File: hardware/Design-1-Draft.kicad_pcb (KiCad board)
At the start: 2 copper layers, 165 x 135 mm, 54 parts, among them J1 Barrel_Jack_Switch, M1 WP-1, M2 WP-2, Q1 IRLZ44N, Q2 IRLZ44N, Q3 PN2222A, SW1 Button, U3 ADS1115, U5 Tang_Nano_9K, U7 BOB-12009

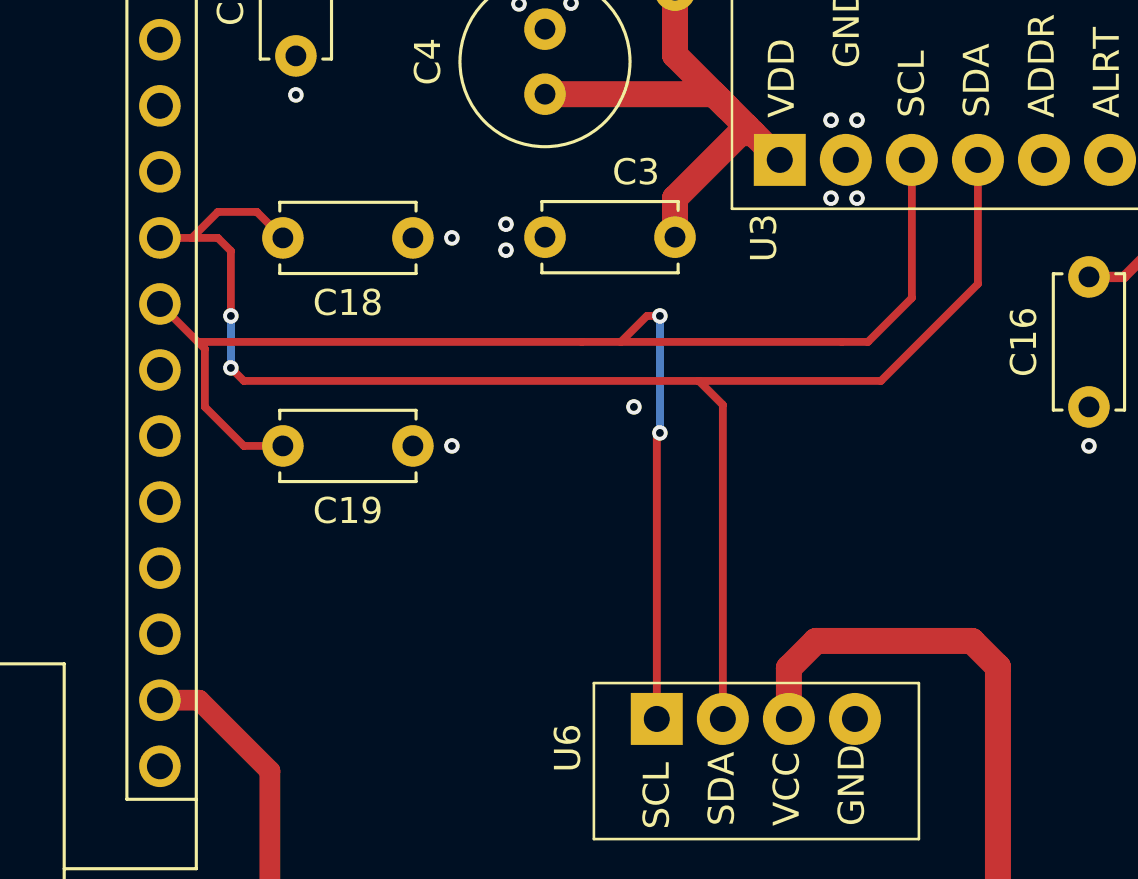
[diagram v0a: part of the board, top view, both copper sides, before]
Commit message: Updated schem & PCB, caps not removed
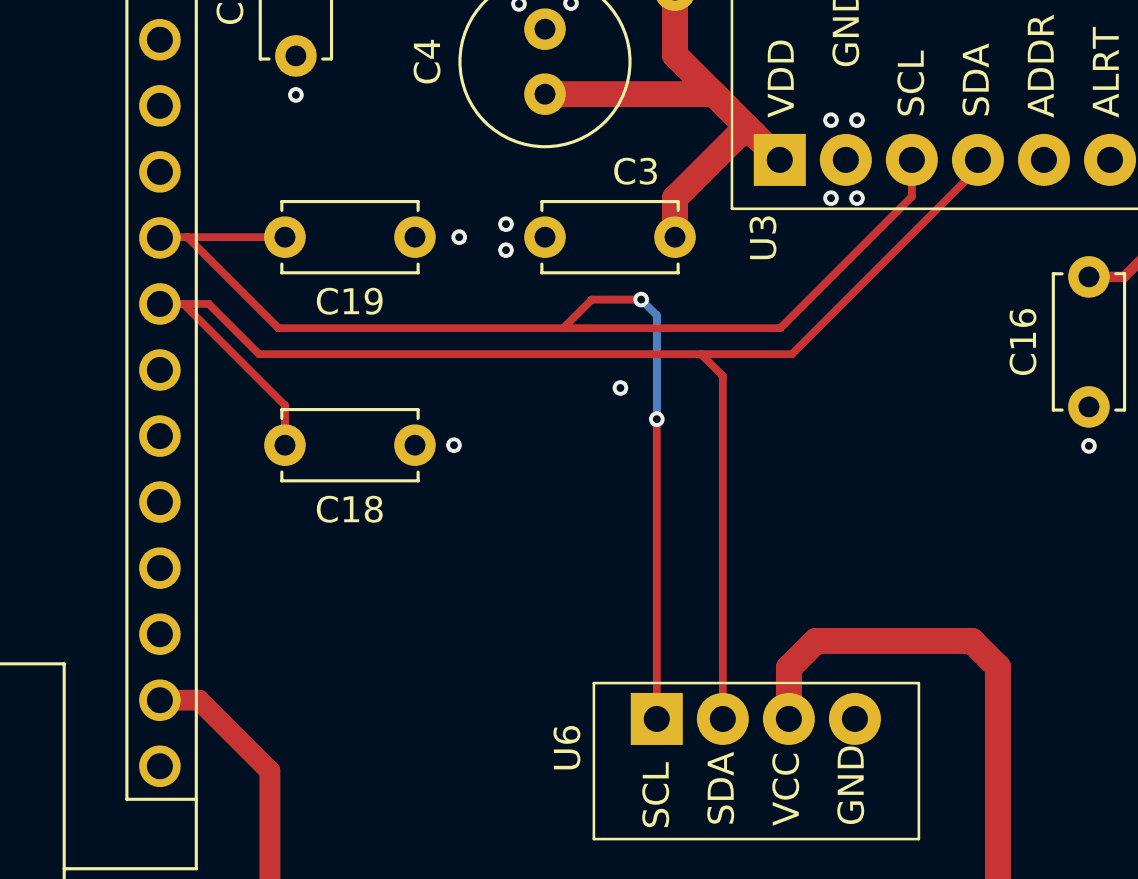
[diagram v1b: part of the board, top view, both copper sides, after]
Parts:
- moved C19 8.03 mm to (143.5, 53.0)
- moved C18 7.97 mm to (143.5, 61.0)
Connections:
- C18 pad 2: Net-(A1-SCL/A5) -> Net-(A1-SDA/A4)
- C19 pad 2: Net-(A1-SDA/A4) -> Net-(A1-SCL/A5)
- U3 pad 10: Net-(A1-SDA/A4) -> Net-(A1-SCL/A5)
- U3 pad 9: Net-(A1-SCL/A5) -> Net-(A1-SDA/A4)
- U6 pad 1: Net-(A1-SDA/A4) -> Net-(A1-SCL/A5)
- U6 pad 2: Net-(A1-SCL/A5) -> Net-(A1-SDA/A4)
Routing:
- net Net-(A1-SCL/A5): track 60.4 -> 57.5 mm
- net Net-(A1-SDA/A4): track 59.2 -> 57.0 mm, vias 2 -> 0
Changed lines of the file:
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@@
 			(layers "*.Cu" "*.Mask")
 			(remove_unused_layers no)
-			(net 7 "Net-(A1-SCL{slash}A5)")
+			(net 4 "Net-(A1-SDA{slash}A4)")
 			(pinfunction "SDA")
 			(pintype "bidirectional")
@@
 			(layers "*.Cu" "*.Mask")
 			(remove_unused_layers no)
-			(net 4 "Net-(A1-SDA{slash}A4)")
+			(net 7 "Net-(A1-SCL{slash}A5)")
 			(pinfunction "SCL")
 			(pintype "input")
@@
 		)
 		(property "Value" "0.1u"
-			(at 2.5 2.5 0)
+			(at 0.9 -2.2 0)
 			(layer "F.Fab")
 			(effects
@@
 	(footprint "Capacitor_THT:C_Disc_D5.0mm_W2.5mm_P5.00mm"
 		(layer "F.Cu")
-		(at 143.42 61.02845 180)
+		(at 143.5 53 180)
 		(descr "C, Disc series, Radial, pin pitch=5.00mm, diameter*width=5*2.5mm^2, Capacitor, http://cdn-reichelt.de/documents/datenblatt/B300/DS_KERKO_TC.pdf")
 		(tags "C Disc series Radial pin pitch 5.00mm diameter 5mm width 2.5mm Capacitor")
@@
 		)
 		(property "Value" "0.1u"
-			(at -3 0 0)
+			(at 2.5 2.5 0)
 			(layer "F.Fab")
 			(effects
@@
 			(layers "*.Cu" "*.Mask")
 			(remove_unused_layers no)
-			(net 4 "Net-(A1-SDA{slash}A4)")
+			(net 7 "Net-(A1-SCL{slash}A5)")
 			(pintype "passive")
 		)
@@
 			(layers "*.Cu" "*.Mask")
 			(remove_unused_layers no)
-			(net 4 "Net-(A1-SDA{slash}A4)")
+			(net 7 "Net-(A1-SCL{slash}A5)")
 			(pinfunction "SCL")
 			(pintype "passive")
@@
 			(layers "*.Cu" "*.Mask")
 			(remove_unused_layers no)
-			(net 7 "Net-(A1-SCL{slash}A5)")
+			(net 4 "Net-(A1-SDA{slash}A4)")
 			(pinfunction "SDA")
 			(pintype "passive")
@@
 	(footprint "Capacitor_THT:C_Disc_D5.0mm_W2.5mm_P5.00mm"
 		(layer "F.Cu")
-		(at 143.42 53.02845 180)
+		(at 143.5 61 180)
 		(descr "C, Disc series, Radial, pin pitch=5.00mm, diameter*width=5*2.5mm^2, Capacitor, http://cdn-reichelt.de/documents/datenblatt/B300/DS_KERKO_TC.pdf")
 		(tags "C Disc series Radial pin pitch 5.00mm diameter 5mm width 2.5mm Capacitor")
@@
 			(layers "*.Cu" "*.Mask")
 			(remove_unused_layers no)
-			(net 7 "Net-(A1-SCL{slash}A5)")
+			(net 4 "Net-(A1-SDA{slash}A4)")
 			(pintype "passive")
 		)
@@
 	)
 	(segment
-		(start 135.42 57.29845)
-		(end 135.15 57.02845)
-		(width 0.3)
-		(layer "F.Cu")
-		(net 4)
-	)
-	(segment
-		(start 138.42 61.02845)
-		(end 136.92 61.02845)
-		(width 0.3)
-		(layer "F.Cu")
-		(net 4)
-	)
-	(segment
-		(start 162.61 50.02845)
-		(end 162.61 55.33845)
-		(width 0.3)
-		(layer "F.Cu")
-		(net 4)
-	)
-	(segment
-		(start 152.92 56.02845)
-		(end 152.42 56.02845)
+		(start 165.15 50.02845)
+		(end 165.15 50.35)
 		(width 0.3)
 		(layer "F.Cu")
@@
 	)
 	(segment
-		(start 152.8 71.52845)
-		(end 152.8 60.64845)
+		(start 135.56845 55.56845)
+		(end 134.6 55.56845)
 		(width 0.3)
 		(layer "F.Cu")
@@
 	)
 	(segment
-		(start 160.92 57.02845)
-		(end 159.92 57.02845)
+		(start 158 57.5)
+		(end 154.5 57.5)
 		(width 0.3)
 		(layer "F.Cu")
@@
 	)
 	(segment
-		(start 152.8 60.64845)
-		(end 152.92 60.52845)
-		(width 0.2)
-		(layer "F.Cu")
-		(net 4)
-	)
-	(segment
-		(start 135.15 57.02845)
-		(end 133.69 55.56845)
+		(start 138.5 61)
+		(end 138.5 59.46845)
 		(width 0.3)
 		(layer "F.Cu")
@@
 	)
 	(segment
-		(start 162.61 55.33845)
-		(end 160.92 57.02845)
+		(start 137.5 57.5)
+		(end 135.56845 55.56845)
 		(width 0.3)
 		(layer "F.Cu")
@@
 	)
 	(segment
-		(start 136.92 61.02845)
-		(end 135.42 59.52845)
+		(start 138.5 59.46845)
+		(end 134.6 55.56845)
 		(width 0.3)
 		(layer "F.Cu")
@@
 	)
 	(segment
-		(start 135.42 59.52845)
-		(end 135.42 57.29845)
+		(start 155.34 58.34)
+		(end 154.5 57.5)
 		(width 0.3)
 		(layer "F.Cu")
@@
 	)
 	(segment
-		(start 152.42 56.02845)
-		(end 151.42 57.02845)
+		(start 155.34 71.52845)
+		(end 155.34 58.34)
 		(width 0.3)
 		(layer "F.Cu")
@@
 	)
 	(segment
-		(start 159.92 57.02845)
-		(end 151.42 57.02845)
+		(start 154.5 57.5)
+		(end 137.5 57.5)
 		(width 0.3)
 		(layer "F.Cu")
@@
 	)
 	(segment
-		(start 151.42 57.02845)
-		(end 149.92 57.02845)
+		(start 134.6 55.56845)
+		(end 133.69 55.56845)
 		(width 0.3)
 		(layer "F.Cu")
@@
 	)
 	(segment
-		(start 149.92 57.02845)
-		(end 135.15 57.02845)
+		(start 165.15 50.35)
+		(end 158 57.5)
 		(width 0.3)
 		(layer "F.Cu")
 		(net 4)
 	)
-	(via
-		(at 152.92 60.52845)
-		(size 0.6)
-		(drill 0.3)
-		(layers "F.Cu" "B.Cu")
-		(net 4)
-	)
-	(via
-		(at 152.92 56.02845)
-		(size 0.6)
-		(drill 0.3)
-		(layers "F.Cu" "B.Cu")
-		(net 4)
-	)
 	(segment
-		(start 152.92 60.52845)
-		(end 152.92 56.02845)
-		(width 0.3)
-		(layer "B.Cu")
-		(net 4)
-	)
-	(segment
-		(start 136.42 53.52845)
-		(end 135.92 53.02845)
-		(width 0.3)
-		(layer "F.Cu")
-		(net 7)
-	)
-	(segment
-		(start 135.92 52.02845)
-		(end 134.92 53.02845)
-		(width 0.3)
-		(layer "F.Cu")
-		(net 7)
-	)
-	(segment
-		(start 138.42 53.02845)
-		(end 137.42 52.02845)
-		(width 0.3)
-		(layer "F.Cu")
-		(net 7)
-	)
-	(segment
-		(start 155.34 59.44845)
-		(end 154.42 58.52845)
+		(start 162.61 50.02845)
+		(end 162.61 51.442663)
 		(width 0.3)
 		(layer "F.Cu")
@@
 	)
 	(segment
-		(start 136.92 58.52845)
-		(end 136.42 58.02845)
+		(start 152.2 55.4)
+		(end 150.3 55.4)
 		(width 0.3)
 		(layer "F.Cu")
@@
 	)
 	(segment
-		(start 155.34 71.52845)
-		(end 155.34 59.44845)
+		(start 138.5 53)
+		(end 134.75 53)
 		(width 0.3)
 		(layer "F.Cu")
@@
 	)
 	(segment
-		(start 165.15 54.79845)
-		(end 161.42 58.52845)
+		(start 162.61 51.442663)
+		(end 157.552663 56.5)
 		(width 0.3)
 		(layer "F.Cu")
@@
 	)
 	(segment
-		(start 154.42 58.52845)
-		(end 136.92 58.52845)
+		(start 134.75 53)
+		(end 133.71845 53)
 		(width 0.3)
 		(layer "F.Cu")
@@
 	)
 	(segment
-		(start 165.15 50.02845)
-		(end 165.15 54.79845)
+		(start 150.3 55.4)
+		(end 149.2 56.5)
 		(width 0.3)
 		(layer "F.Cu")
@@
 	)
 	(segment
-		(start 136.42 56.02845)
-		(end 136.42 53.52845)
+		(start 138.25 56.5)
+		(end 134.75 53)
 		(width 0.3)
 		(layer "F.Cu")
@@
 	)
 	(segment
-		(start 135.92 53.02845)
-		(end 134.92 53.02845)
+		(start 149.2 56.5)
+		(end 138.25 56.5)
 		(width 0.3)
 		(layer "F.Cu")
@@
 	)
 	(segment
-		(start 137.42 52.02845)
-		(end 135.92 52.02845)
+		(start 152.8 71.52845)
+		(end 152.8 60)
 		(width 0.3)
 		(layer "F.Cu")
@@
 	)
 	(segment
-		(start 161.42 58.52845)
-		(end 154.42 58.52845)
+		(start 133.71845 53)
+		(end 133.69 53.02845)
 		(width 0.3)
 		(layer "F.Cu")
@@
 	)
 	(segment
-		(start 134.92 53.02845)
-		(end 133.69 53.02845)
+		(start 157.552663 56.5)
+		(end 149.2 56.5)
 		(width 0.3)
 		(layer "F.Cu")
@@
 	)
 	(via
-		(at 136.42 58.02845)
+		(at 152.8 60)
 		(size 0.6)
 		(drill 0.3)
@@
 	)
 	(via
-		(at 136.42 56.02845)
+		(at 152.2 55.4)
 		(size 0.6)
 		(drill 0.3)
@@
 	)
 	(segment
-		(start 136.42 58.02845)
-		(end 136.42 56.02845)
+		(start 152.8 60)
+		(end 152.8 56)
+		(width 0.3)
+		(layer "B.Cu")
+		(net 7)
+	)
+	(segment
+		(start 152.8 56)
+		(end 152.2 55.4)
 		(width 0.3)
 		(layer "B.Cu")
@@
 	)
 	(via
-		(at 151.92 59.52845)
+		(at 151.4 58.8)
 		(size 0.6)
 		(drill 0.3)
@@
 	)
 	(via
-		(at 144.92 61.02845)
+		(at 145.2 53)
 		(size 0.6)
 		(drill 0.3)
@@
 	)
 	(via
-		(at 144.92 53.02845)
+		(at 145 61)
 		(size 0.6)
 		(drill 0.3)
